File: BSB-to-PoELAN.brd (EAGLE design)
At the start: 86.5 x 49.4 mm, 123 parts, among them IC1 LAN8710A-EZC, IC2 TPS2376DDA, IC3 TX4138, IC4 SY8089AAAC, IC6 CH340X, Q1 BC847, Q2 BC857, Q3 BC847, Q4 WPM2015-3/TR, Q5 BC847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

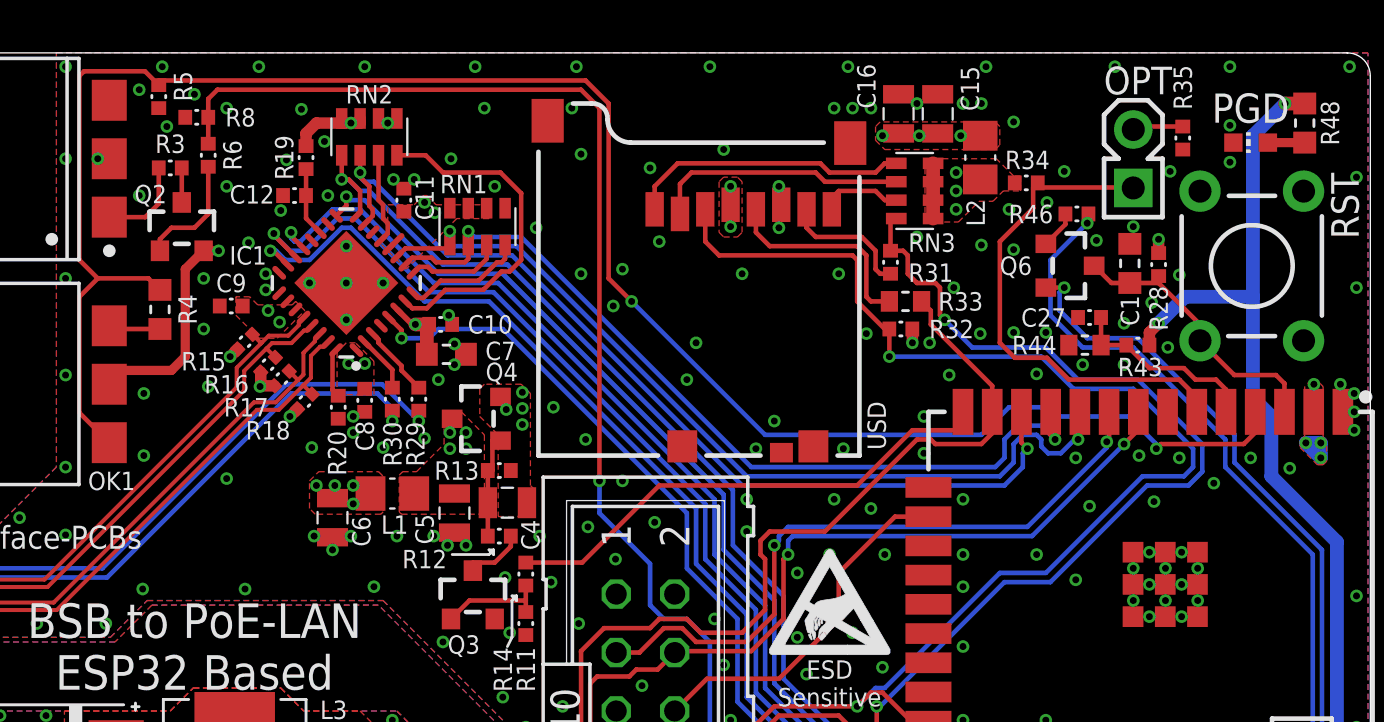
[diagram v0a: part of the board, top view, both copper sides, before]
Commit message: Add BSB Tx Enable Control
Move the UEXT RX on GPIO35 (input only), and use GPIO32 instead for controlling whether the BSB-TXD pin can drive the optocoupler. This basically replaces the +3.3V connection on the emitter of the invert transistor.

What this means is that when the ESP32 has not yet booted, or if it crashes along the way, the BSB bus is not being driven into TX mode by the pull-down bootstrap resistor. This should stop BSB bus short detection errors when the unit is powered off or has not yet started up.

This will require custom code in the BSB firmware setup (BSB_LAN_custom_setup.h) to configure the enable pin to be an output and driven high. Until that is done the BSB bus remains passive.
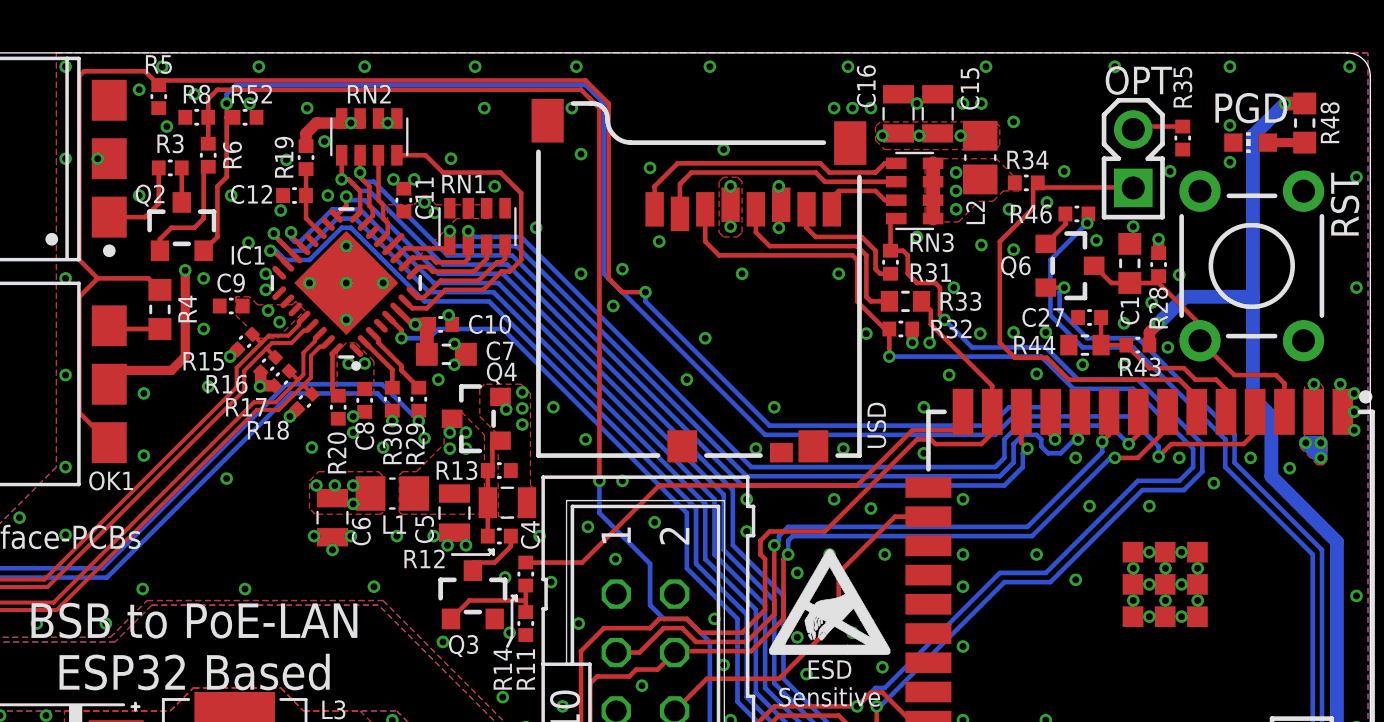
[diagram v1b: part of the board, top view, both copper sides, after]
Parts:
- added R52: 4.7k, BSB-LAN:R0402
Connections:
- new net BSB-ENB: ESP1.8, Q2.E, R52.2
- net +3.3V: no longer Q2.E
- net GND: now also R52.1
- net UEXT-RX: now also ESP1.7; no longer ESP1.8
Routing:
- net BSB-ENB: track 0.00 -> 59.9 mm, vias 0 -> 2
- net UEXT-RX: track 47.7 -> 48.9 mm
- net +3.3V: track 49.0 -> 48.4 mm
- net GND: vias 319 -> 318
